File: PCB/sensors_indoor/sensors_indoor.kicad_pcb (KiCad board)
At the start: 4 copper layers, 50 x 50 mm, 45 parts, among them J1 USB4125-GF-A, J2 STDC14, J3 B5B-ZR, SW1 TL3305, U1 MIC5219-3.3YM5, U2 STM32WBA5MMG, U3 FM24CL16B, U4 SHT45-AD1F, U5 SCD41-D-R2, U6 SGP41, U7 OPT4001DNPRQ1

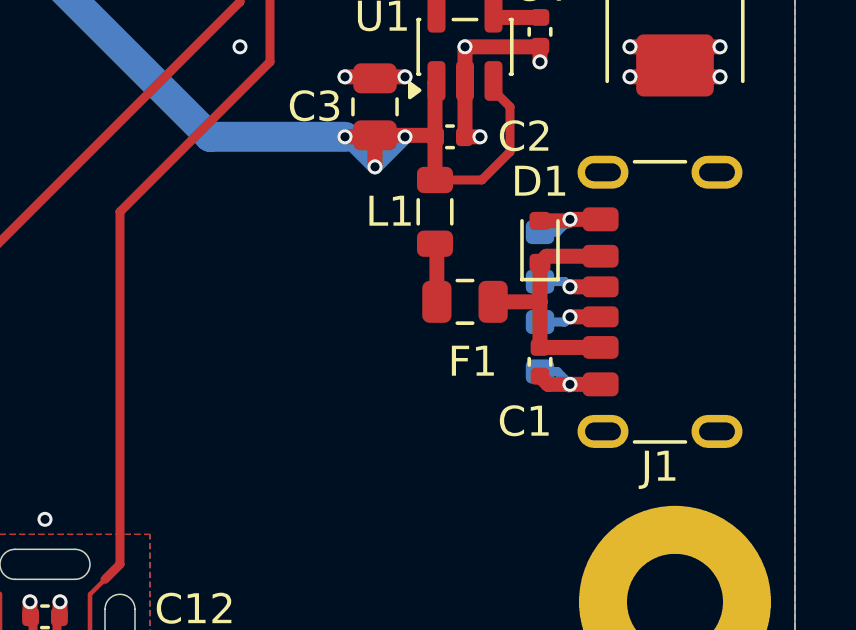
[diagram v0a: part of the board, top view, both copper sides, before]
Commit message: Changed PTC fuse part
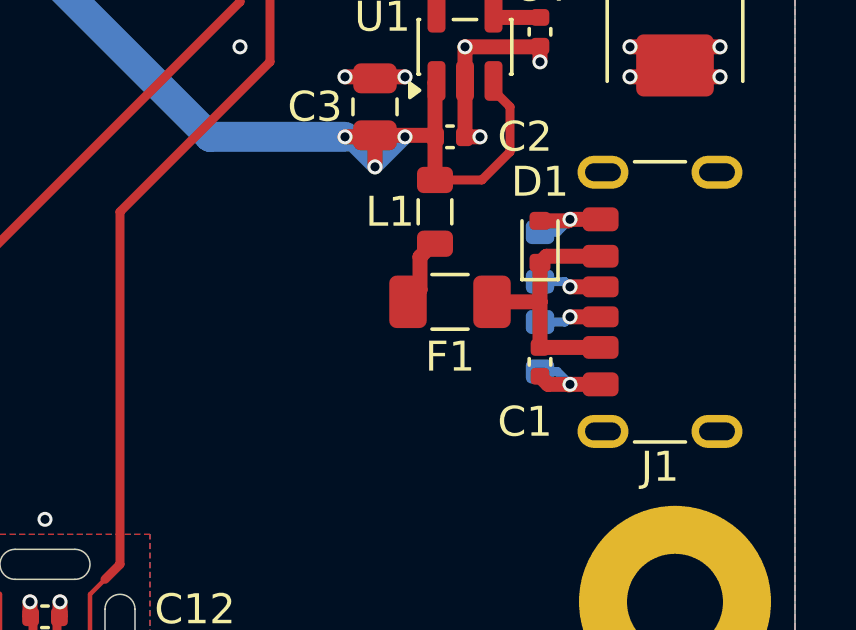
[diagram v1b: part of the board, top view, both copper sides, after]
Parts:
- F1: footprint Fuse:Fuse_0805_2012Metric -> Fuse:Fuse_1206_3216Metric
- moved F1 0.50 mm to (113.5, 111.0)
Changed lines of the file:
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@@
 		)
 	)
-	(footprint "Fuse:Fuse_0805_2012Metric"
+	(footprint "Fuse:Fuse_1206_3216Metric"
 		(layer "F.Cu")
-		(at 114 111 180)
-		(descr "Fuse SMD 0805 (2012 Metric), square (rectangular) end terminal, IPC-7351 nominal, (Body size source: https://docs.google.com/spreadsheets/d/1BsfQQcO9C6DZCsRaXUlFlo91Tg2WpOkGARC1WS5S8t0/edit?usp=sharing), generated with kicad-footprint-generator")
+		(at 113.5 111 180)
+		(descr "Fuse SMD 1206 (3216 Metric), square (rectangular) end terminal, IPC-7351 nominal, (Body size source: http://www.tortai-tech.com/upload/download/2011102023233369053.pdf), generated with kicad-footprint-generator")
 		(tags "fuse")
 		(property "Reference" "F1"
-			(at -0.258578 -2 0)
+			(at 0 -1.83 180)
 			(layer "F.SilkS")
 			(effects
@@
 		)
 		(property "Value" "500mA"
-			(at 0 1.65 0)
+			(at 0 1.83 180)
 			(layer "F.Fab")
 			(effects
@@
 		)
 		(property "Datasheet" "~"
-			(at 0 0 0)
+			(at 0 0 180)
 			(layer "F.Fab")
 			(hide yes)
@@
 		)
 		(property "Description" "Resettable fuse, polymeric positive temperature coefficient"
-			(at 0 0 0)
+			(at 0 0 180)
 			(layer "F.Fab")
 			(hide yes)
@@
 			)
 		)
+		(property "MPN" "MF-NSMF050-2"
+			(at 0 0 180)
+			(unlocked yes)
+			(layer "F.Fab")
+			(hide yes)
+			(effects
+				(font
+					(size 1 1)
+					(thickness 0.15)
+				)
+			)
+		)
+		(property "Mouser PN" "652-MF-NSMF050-2"
+			(at 0 0 180)
+			(unlocked yes)
+			(layer "F.Fab")
+			(hide yes)
+			(effects
+				(font
+					(size 1 1)
+					(thickness 0.15)
+				)
+			)
+		)
 		(property ki_fp_filters "*polyfuse* *PTC*")
 		(sheetname "/")
@@
 		(attr smd)
 		(fp_line
-			(start -0.258578 0.71)
-			(end 0.258578 0.71)
+			(start -0.602064 0.91)
+			(end 0.602064 0.91)
 			(stroke
 				(width 0.12)
@@
 		)
 		(fp_line
-			(start -0.258578 -0.71)
-			(end 0.258578 -0.71)
+			(start -0.602064 -0.91)
+			(end 0.602064 -0.91)
 			(stroke
 				(width 0.12)
@@
 		)
 		(fp_line
-			(start 1.68 0.95)
-			(end -1.68 0.95)
+			(start 2.28 1.13)
+			(end -2.28 1.13)
 			(stroke
 				(width 0.05)
@@
 		)
 		(fp_line
-			(start 1.68 -0.95)
-			(end 1.68 0.95)
+			(start 2.28 -1.13)
+			(end 2.28 1.13)
 			(stroke
 				(width 0.05)
@@
 		)
 		(fp_line
-			(start -1.68 0.95)
-			(end -1.68 -0.95)
+			(start -2.28 1.13)
+			(end -2.28 -1.13)
 			(stroke
 				(width 0.05)
@@
 		)
 		(fp_line
-			(start -1.68 -0.95)
-			(end 1.68 -0.95)
+			(start -2.28 -1.13)
+			(end 2.28 -1.13)
 			(stroke
 				(width 0.05)
@@
 		)
 		(fp_line
-			(start 1 0.6)
-			(end -1 0.6)
+			(start 1.6 0.8)
+			(end -1.6 0.8)
 			(stroke
 				(width 0.1)
@@
 		)
 		(fp_line
-			(start 1 -0.6)
-			(end 1 0.6)
+			(start 1.6 -0.8)
+			(end 1.6 0.8)
 			(stroke
 				(width 0.1)
@@
 		)
 		(fp_line
-			(start -1 0.6)
-			(end -1 -0.6)
+			(start -1.6 0.8)
+			(end -1.6 -0.8)
 			(stroke
 				(width 0.1)
@@
 		)
 		(fp_line
-			(start -1 -0.6)
-			(end 1 -0.6)
+			(start -1.6 -0.8)
+			(end 1.6 -0.8)
 			(stroke
 				(width 0.1)
@@
 		)
 		(fp_text user "${REFERENCE}"
-			(at 0 0 0)
+			(at 0 0 180)
 			(layer "F.Fab")
 			(effects
 				(font
-					(size 0.5 0.5)
-					(thickness 0.08)
+					(size 0.8 0.8)
+					(thickness 0.12)
 				)
 			)
 		)
 		(pad "1" smd roundrect
-			(at -0.9375 0 180)
-			(size 0.975 1.4)
+			(at -1.4 0 180)
+			(size 1.25 1.75)
 			(layers "F.Cu" "F.Mask" "F.Paste")
-			(roundrect_rratio 0.25)
+			(roundrect_rratio 0.2)
 			(net 1 "/VBUS")
 			(pintype "passive")
 		)
 		(pad "2" smd roundrect
-			(at 0.9375 0 180)
-			(size 0.975 1.4)
+			(at 1.4 0 180)
+			(size 1.25 1.75)
 			(layers "F.Cu" "F.Mask" "F.Paste")
-			(roundrect_rratio 0.25)
+			(roundrect_rratio 0.2)
 			(net 34 "Net-(F1-Pad2)")
 			(pintype "passive")
 		)
 		(embedded_fonts no)
-		(model "${KICAD9_3DMODEL_DIR}/Fuse.3dshapes/Fuse_0805_2012Metric.step"
+		(model "${KICAD9_3DMODEL_DIR}/Fuse.3dshapes/Fuse_1206_3216Metric.step"
 			(offset
 				(xyz 0 0 0)
@@
 	)
 	(segment
-		(start 113.0625 111)
-		(end 113.0625 109.125)
+		(start 112.1 111)
+		(end 112.5 110.6)
 		(width 0.5)
 		(layer "F.Cu")
@@
 	)
 	(segment
-		(start 113.0625 109.125)
+		(start 112.5 110.6)
+		(end 112.5 109.5)
+		(width 0.5)
+		(layer "F.Cu")
+		(net 34)
+	)
+	(segment
+		(start 112.9375 109.0625)
 		(end 113 109.0625)
 		(width 0.5)
 		(layer "F.Cu")
+		(net 34)
+	)
+	(segment
+		(start 112.5 109.5)
+		(end 112.9375 109.0625)
+		(width 0.5)
+		(layer "F.Cu")

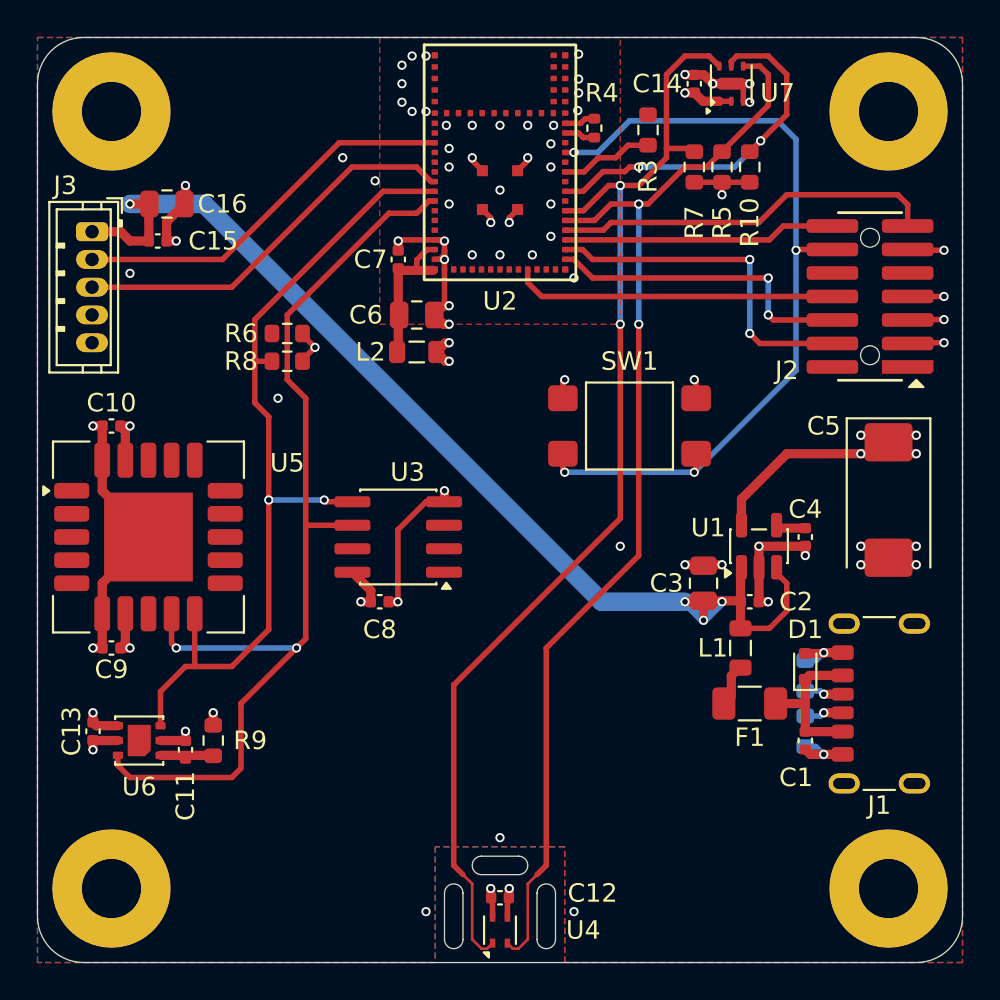
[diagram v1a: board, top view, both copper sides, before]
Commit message: Added LEDs
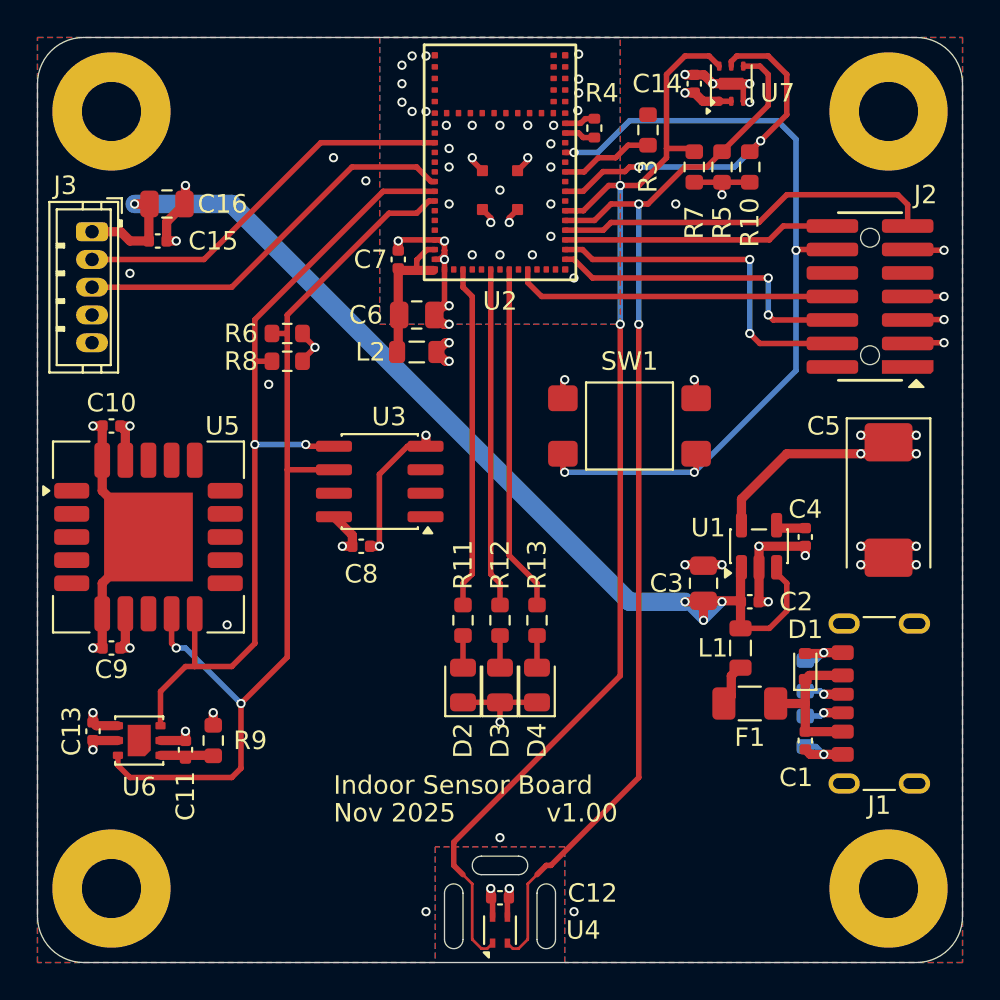
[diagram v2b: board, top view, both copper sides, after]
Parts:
- added D2: RED, LED_SMD:LED_0805_2012Metric, F.Cu at (98.0, 110.0)
- added D3: YEL, LED_SMD:LED_0805_2012Metric, F.Cu at (100.0, 110.0)
- added D4: GRN, LED_SMD:LED_0805_2012Metric, F.Cu at (102.0, 110.0)
- added R11: 270R, Resistor_SMD:R_0603_1608Metric, F.Cu at (98.0, 106.5)
- added R12: 270R, Resistor_SMD:R_0603_1608Metric, F.Cu at (100.0, 106.5)
- added R13: 270R, Resistor_SMD:R_0603_1608Metric, F.Cu at (102.0, 106.5)
- moved C8 3.16 mm to (92.5, 102.5)
- moved U3 3.16 mm to (93.5, 99.0)
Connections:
- U2 pad 25: unconnected-(U2-PA2-Pad25) -> /MCU/LED0
- U2 pad 28: unconnected-(U2-PC13-Pad28) -> /MCU/LED1
- U2 pad 30: unconnected-(U2-PB6-Pad30) -> /MCU/LED2
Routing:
- net /MCU/LED2: track 0.00 -> 18.8 mm
- net /MCU/LED0: track 0.00 -> 18.5 mm
- net /MCU/LED1: track 0.00 -> 18.3 mm
- net GND: track 86.8 -> 91.9 mm, vias 74 -> 76
- net I2C3_SCL: track 55.5 -> 53.8 mm
- net Net-(D4-A): track 0.00 -> 1.74 mm
- net Net-(D3-A): track 0.00 -> 1.74 mm
- net Net-(D2-A): track 0.00 -> 1.74 mm
- net I2C3_SDA: track 47.1 -> 46.2 mm
- net +5V: track 61.0 -> 60.5 mm
- added copper zone on In2.Cu, net GND
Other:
- board text added: "Indoor Sensor Board"
- board text added: "Nov 2025"
- board text added: "v1.00"

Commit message: Rotated USB-C to exit at bottom, added debug pins for I2C
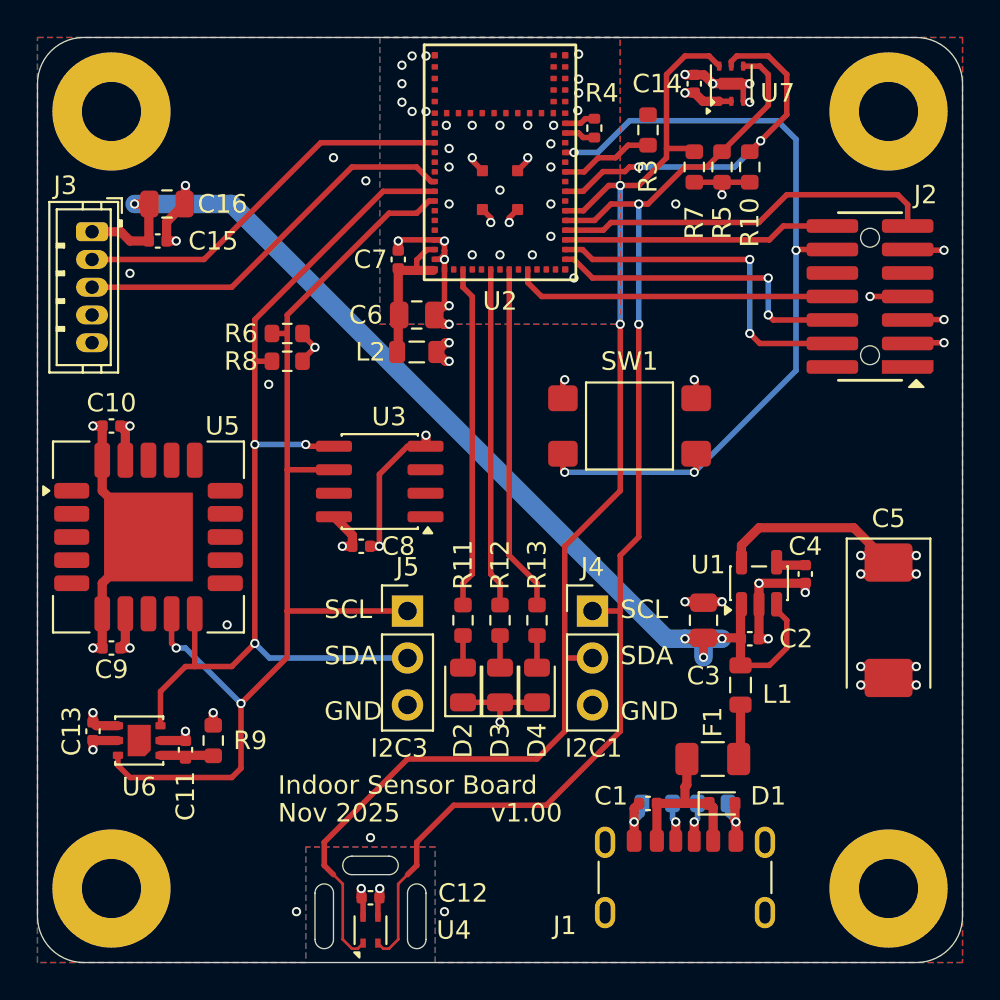
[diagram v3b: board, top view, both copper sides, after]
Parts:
- added J4: Conn_01x03, Connector_PinHeader_2.54mm:PinHeader_1x03_P2.54mm_Vertical, F.Cu at (105.0, 106.0)
- added J5: Conn_01x03, Connector_PinHeader_2.54mm:PinHeader_1x03_P2.54mm_Vertical, F.Cu at (95.0, 106.0)
- moved J1 15.6 mm to (110.0, 121.5), turned to 0 degrees
- moved C1 9.15 mm to (108.0, 116.4), turned to 180 degrees
- moved R2 8.90 mm to (108.5, 116.4), turned to 180 degrees
- moved D1 8.66 mm to (112.0, 116.4), turned to 0 degrees
- moved R1 8.52 mm to (111.5, 116.4), turned to 0 degrees
- moved C12 7.00 mm to (93.0, 121.5)
- moved U4 7.00 mm to (93.0, 123.2)
- moved C5 6.50 mm to (121.0, 106.5)
- moved F1 3.61 mm to (111.5, 114.0), turned to 0 degrees
- moved C2 2.00 mm to (113.5, 107.5)
- moved C3 2.00 mm to (111.0, 106.5)
- moved C4 2.00 mm to (116.5, 104.0)
- moved L1 2.00 mm to (113.0, 110.0)
- moved U1 2.00 mm to (114.0, 104.5)
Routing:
- net I2C3_SDA: track 46.2 -> 54.8 mm, vias 2 -> 3
- net I2C1_SDA: track 62.6 -> 71.1 mm
- net I2C1_SCL: track 60.6 -> 67.8 mm
- net I2C3_SCL: track 53.8 -> 60.3 mm
- net +3.3V: track 43.5 -> 44.6 mm
- net +5V: track 60.5 -> 61.5 mm
- net /VBUS: track 8.51 -> 9.39 mm
- net Net-(F1-Pad2): track 2.35 -> 3.03 mm
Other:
- outline, holes or cut-outs redrawn
- board text added: "GND"
- board text added: "I2C1"
- board text added: "I2C3"
- board text added: "SCL"
- board text added: "SDA"
